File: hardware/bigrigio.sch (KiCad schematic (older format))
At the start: 3 parts

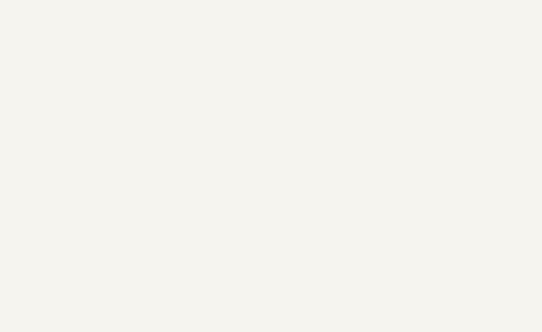
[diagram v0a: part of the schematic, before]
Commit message: h bridge driver schematic symbol added
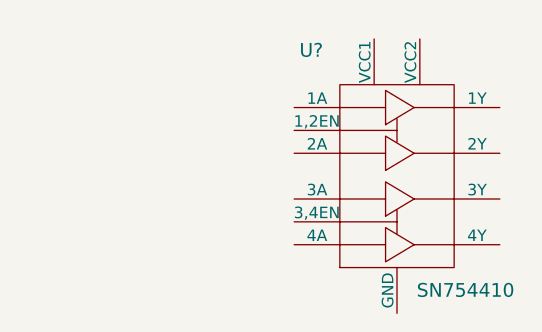
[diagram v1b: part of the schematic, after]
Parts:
- added U?: SN754410, symbol SN754410
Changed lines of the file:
@@
 LIBS:valves
 LIBS:bigrigio
+LIBS:bigrigio-cache
 EELAYER 25 0
 EELAYER END
@@
 	1    0    0    -1
 $EndComp
+$Comp
+L SN754410 U?
+U 1 1 5CE9AB26
+P 7750 2500
+F 0 "U?" H 7375 3050 60  0000 C CNN
+F 1 "SN754410" H 8050 2000 60  0000 C CNN
+F 2 "" H 7750 2500 60  0000 C CNN
+F 3 "" H 7750 2500 60  0000 C CNN
+	1    7750 2500
+	1    0    0    -1
+$EndComp

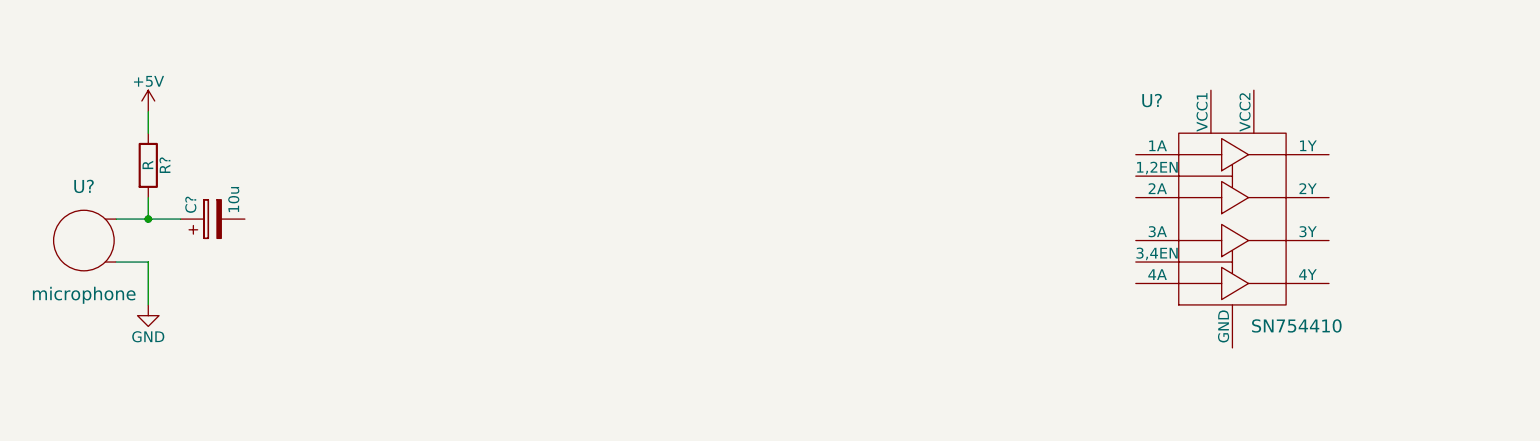
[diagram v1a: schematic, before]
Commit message: H bridge chip wiring
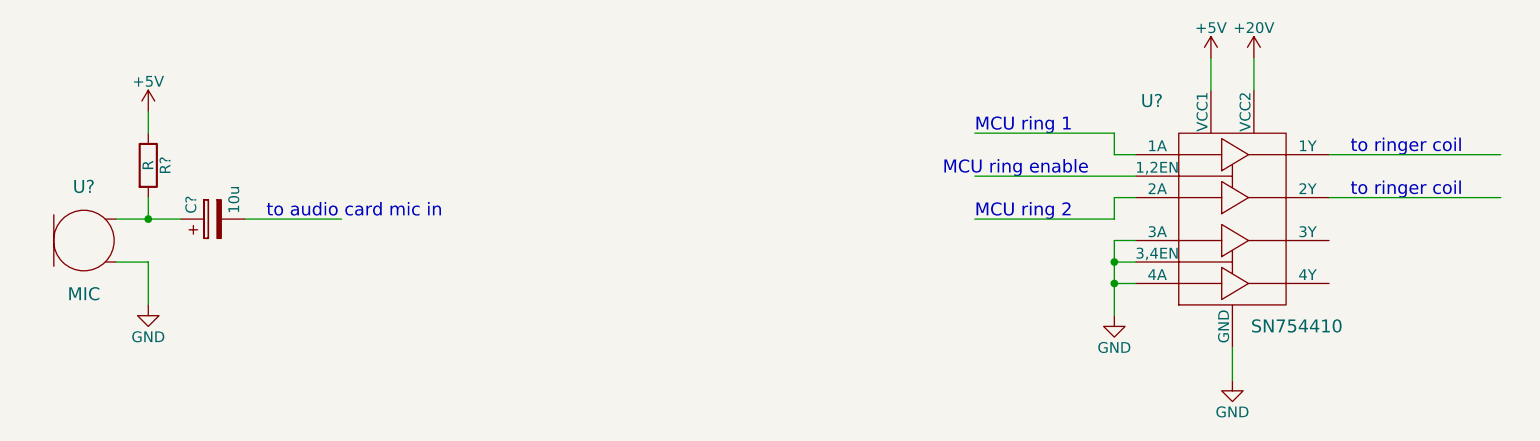
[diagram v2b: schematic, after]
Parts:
- removed U?: microphone, symbol microphone
- added U?: MIC, symbol MIC
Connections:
- net labels added: +20V
- wire segments 5 -> 22
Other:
- note added: "MCU ring 1\n"
- note added: "MCU ring 2"
- note added: "MCU ring enable"
- note added: "to audio card mic in"
- note added: "to ringer coil"
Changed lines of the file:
@@
+	1    0    0    -1
+$EndComp
+$Comp
+L SN754410 U?
+U 1 1 5CE9AB26
+P 7750 2500
+F 0 "U?" H 7375 3050 60  0000 C CNN
+F 1 "SN754410" H 8050 2000 60  0000 C CNN
+F 2 "" H 7750 2500 60  0000 C CNN
+F 3 "" H 7750 2500 60  0000 C CNN
+	1    7750 2500
+	1    0    0    -1
+$EndComp
+$Comp
+L GND #PWR?
+U 1 1 5CEAA1E6
+P 7750 3250
+F 0 "#PWR?" H 7750 3000 50  0001 C CNN
+F 1 "GND" H 7750 3100 50  0000 C CNN
+F 2 "" H 7750 3250 50  0000 C CNN
+F 3 "" H 7750 3250 50  0000 C CNN
+	1    7750 3250
+	1    0    0    -1
+$EndComp
+$Comp
+L GND #PWR?
+U 1 1 5CEAA20E
+P 7200 2950
+F 0 "#PWR?" H 7200 2700 50  0001 C CNN
+F 1 "GND" H 7200 2800 50  0000 C CNN
+F 2 "" H 7200 2950 50  0000 C CNN
+F 3 "" H 7200 2950 50  0000 C CNN
+	1    7200 2950
+	1    0    0    -1
+$EndComp
+$Comp
+L +20V #PWR?
+U 1 1 5CEAA347
+P 7850 1750
+F 0 "#PWR?" H 7850 1600 50  0001 C CNN
+F 1 "+20V" H 7850 1890 50  0000 C CNN
+F 2 "" H 7850 1750 50  0000 C CNN
+F 3 "" H 7850 1750 50  0000 C CNN
+	1    7850 1750
+	1    0    0    -1
+$EndComp
+$Comp
+L +5V #PWR?
+U 1 1 5CEAA367
+P 7650 1750
+F 0 "#PWR?" H 7650 1600 50  0001 C CNN
+F 1 "+5V" H 7650 1890 50  0000 C CNN
+F 2 "" H 7650 1750 50  0000 C CNN
+F 3 "" H 7650 1750 50  0000 C CNN
+	1    7650 1750
 	1    0    0    -1
 $EndComp
@@
 Wire Wire Line
 	2700 2700 2700 2900
+Wire Wire Line
+	7750 3250 7750 3100
+Wire Wire Line
+	7200 2600 7200 2950
+Wire Wire Line
+	7200 2800 7300 2800
+Wire Wire Line
+	7200 2700 7300 2700
+Connection ~ 7200 2800
+Wire Wire Line
+	7200 2600 7300 2600
+Connection ~ 7200 2700
+Wire Wire Line
+	7650 1750 7650 1900
+Wire Wire Line
+	7850 1900 7850 1750
+Wire Wire Line
+	8200 2200 9000 2200
+Wire Wire Line
+	8200 2400 9000 2400
+Text Notes 8300 2200 0    60   ~ 0
+to ringer coil
+Text Notes 8300 2400 0    60   ~ 0
+to ringer coil
+Wire Wire Line
+	7300 2200 7200 2200
+Wire Wire Line
+	7200 2200 7200 2100
+Wire Wire Line
+	7200 2100 6550 2100
+Wire Wire Line
+	7300 2300 6550 2300
+Wire Wire Line
+	7300 2400 7200 2400
+Wire Wire Line
+	7200 2400 7200 2500
+Wire Wire Line
+	7200 2500 6550 2500
+Text Notes 6550 2100 0    60   ~ 0
+MCU ring 1\n
+Text Notes 6550 2500 0    60   ~ 0
+MCU ring 2
+Text Notes 6400 2300 0    60   ~ 0
+MCU ring enable
 $Comp
-L microphone U?
-U 1 1 5CE97E98
+L MIC U?
+U 1 1 5CEAA888
 P 2400 2600
 F 0 "U?" H 2400 2850 60  0000 C CNN
-F 1 "microphone" H 2400 2350 60  0000 C CNN
+F 1 "MIC" H 2400 2350 60  0000 C CNN
 F 2 "" H 2400 2600 60  0000 C CNN
 F 3 "" H 2400 2600 60  0000 C CNN
@@
 	1    0    0    -1
 $EndComp
-$Comp
-L SN754410 U?
-U 1 1 5CE9AB26
-P 7750 2500
-F 0 "U?" H 7375 3050 60  0000 C CNN
-F 1 "SN754410" H 8050 2000 60  0000 C CNN
-F 2 "" H 7750 2500 60  0000 C CNN
-F 3 "" H 7750 2500 60  0000 C CNN
-	1    7750 2500
-	1    0    0    -1
-$EndComp
+Wire Wire Line
+	3150 2500 3600 2500
+Text Notes 3250 2500 0    60   ~ 0
+to audio card mic in
 $EndSCHEMATC
